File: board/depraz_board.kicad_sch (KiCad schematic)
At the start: 30 parts, among them J1 Switches, J2 Host, J3 SWD, U1 TLV75519PDRV, U2 TLV75533PDRV, U5 PMW3389DM, U6 STM32F103C8Tx, Y1 Crystal

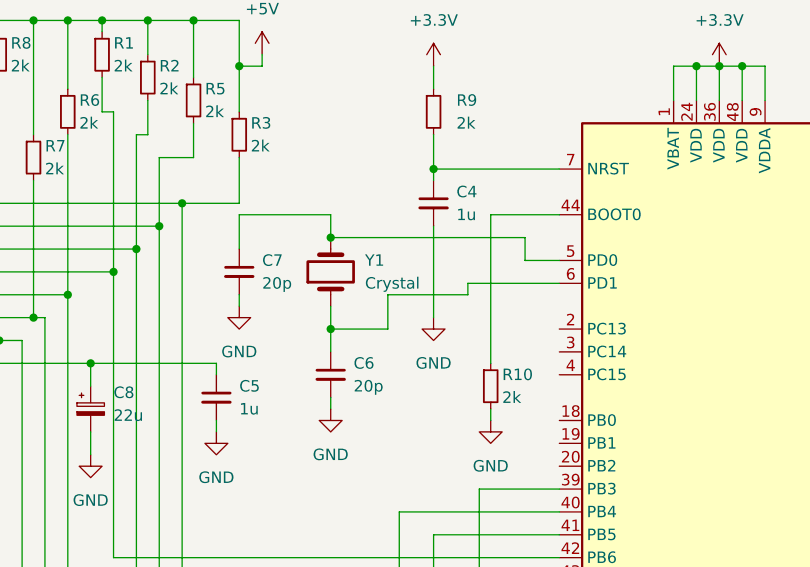
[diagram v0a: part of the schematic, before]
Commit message: Added LCSC part numbers for the SMD parts.
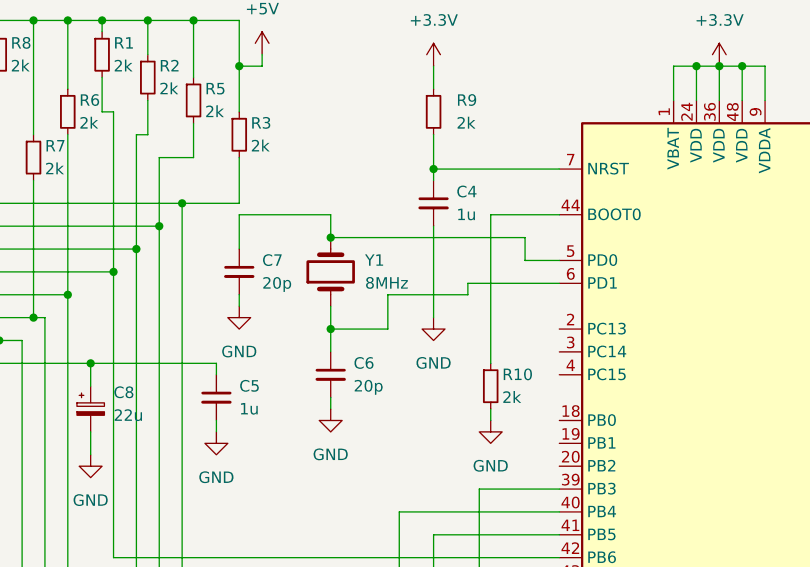
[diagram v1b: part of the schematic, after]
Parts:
- C1, C3, C4, C5: LCSC (none) -> C28323
- C2: LCSC (none) -> C1779
- C6, C7: LCSC (none) -> C1554
- C8: LCSC (none) -> C335975
- R1, R10, R2, R3, R5, R6, R7, R8, R9: LCSC (none) -> C4109
- R4: LCSC (none) -> C25282
- U1: LCSC (none) -> C2861631
- U2: LCSC (none) -> C2861750
- U6: LCSC (none) -> C8734
- Y1: value Crystal -> 8MHz; LCSC (none) -> C20617538
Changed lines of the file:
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@@
 			)
 		)
+		(property "LCSC" "C1779"
+			(at 266.7 102.87 0)
+			(effects
+				(font
+					(size 1.27 1.27)
+				)
+				(hide yes)
+			)
+		)
 		(pin "1"
 		)
@@
 			)
 		)
+		(property "LCSC" "C25282"
+			(at 214.63 107.95 90)
+			(effects
+				(font
+					(size 1.27 1.27)
+				)
+				(hide yes)
+			)
+		)
 		(pin "2"
 		)
@@
 			)
 		)
+		(property "LCSC" "C2861750"
+			(at 181.61 33.02 0)
+			(effects
+				(font
+					(size 1.27 1.27)
+				)
+				(hide yes)
+			)
+		)
 		(pin "6"
 		)
@@
 			)
 		)
+		(property "LCSC" "C1554"
+			(at 80.01 57.15 0)
+			(effects
+				(font
+					(size 1.27 1.27)
+				)
+				(hide yes)
+			)
+		)
 		(pin "1"
 		)
@@
 			)
 		)
+		(property "LCSC" "C4109"
+			(at 43.18 21.59 0)
+			(effects
+				(font
+					(size 1.27 1.27)
+				)
+				(hide yes)
+			)
+		)
 		(pin "1"
 		)
@@
 			)
 		)
+		(property "LCSC" "C8734"
+			(at 123.19 67.31 0)
+			(effects
+				(font
+					(size 1.27 1.27)
+				)
+				(hide yes)
+			)
+		)
 		(pin "47"
 		)
@@
 			)
 		)
+		(property "LCSC" "C4109"
+			(at 50.8 27.94 0)
+			(effects
+				(font
+					(size 1.27 1.27)
+				)
+				(hide yes)
+			)
+		)
 		(pin "1"
 		)
@@
 			)
 		)
+		(property "LCSC" "C4109"
+			(at 54.61 21.59 0)
+			(effects
+				(font
+					(size 1.27 1.27)
+				)
+				(hide yes)
+			)
+		)
 		(pin "1"
 		)
@@
 			)
 		)
+		(property "LCSC" "C28323"
+			(at 191.77 35.56 0)
+			(effects
+				(font
+					(size 1.27 1.27)
+				)
+				(hide yes)
+			)
+		)
 		(pin "1"
 		)
@@
 			)
 		)
+		(property "LCSC" "C4109"
+			(at 91.44 27.94 0)
+			(effects
+				(font
+					(size 1.27 1.27)
+				)
+				(hide yes)
+			)
+		)
 		(pin "2"
 		)
@@
 			)
 		)
+		(property "LCSC" "C4109"
+			(at 64.77 26.67 0)
+			(effects
+				(font
+					(size 1.27 1.27)
+				)
+				(hide yes)
+			)
+		)
 		(pin "1"
 		)
@@
 			)
 		)
+		(property "LCSC" "C4109"
+			(at 97.79 58.42 0)
+			(effects
+				(font
+					(size 1.27 1.27)
+				)
+				(hide yes)
+			)
+		)
 		(pin "1"
 		)
@@
 			)
 		)
+		(property "LCSC" "C28323"
+			(at 67.31 59.69 0)
+			(effects
+				(font
+					(size 1.27 1.27)
+				)
+				(hide yes)
+			)
+		)
 		(pin "1"
 		)
@@
 			)
 		)
+		(property "LCSC" "C28323"
+			(at 222.25 35.56 0)
+			(effects
+				(font
+					(size 1.27 1.27)
+				)
+				(hide yes)
+			)
+		)
 		(pin "2"
 		)
@@
 			)
 		)
+		(property "LCSC" "C1554"
+			(at 69.85 45.72 0)
+			(effects
+				(font
+					(size 1.27 1.27)
+				)
+				(hide yes)
+			)
+		)
 		(pin "1"
 		)
@@
 			)
 		)
+		(property "LCSC" "C28323"
+			(at 91.44 38.1 0)
+			(effects
+				(font
+					(size 1.27 1.27)
+				)
+				(hide yes)
+			)
+		)
 		(pin "1"
 		)
@@
 			)
 		)
+		(property "LCSC" "C4109"
+			(at 59.69 24.13 0)
+			(effects
+				(font
+					(size 1.27 1.27)
+				)
+				(hide yes)
+			)
+		)
 		(pin "1"
 		)
@@
 			)
 		)
+		(property "LCSC" "C335975"
+			(at 53.34 60.96 0)
+			(effects
+				(font
+					(size 1.27 1.27)
+				)
+				(hide yes)
+			)
+		)
 		(pin "1"
 		)
@@
 			)
 		)
+		(property "LCSC" "C4109"
+			(at 46.99 33.02 0)
+			(effects
+				(font
+					(size 1.27 1.27)
+				)
+				(hide yes)
+			)
+		)
 		(pin "1"
 		)
@@
 			)
 		)
-		(property "Value" "Crystal"
+		(property "Value" "8MHz"
 			(at 83.82 46.9899 90)
 			(effects
@@
 			)
 		)
+		(property "LCSC" "C20617538"
+			(at 80.01 45.72 90)
+			(effects
+				(font
+					(size 1.27 1.27)
+				)
+				(hide yes)
+			)
+		)
 		(pin "2"
 		)
@@
 			)
 		)
+		(property "LCSC" "C4109"
+			(at 69.85 30.48 0)
+			(effects
+				(font
+					(size 1.27 1.27)
+				)
+				(hide yes)
+			)
+		)
 		(pin "1"
 		)
@@
 			(at 210.82 33.02 0)
 			(effects
+				(font
+					(size 1.27 1.27)
+				)
+				(hide yes)
+			)
+		)
+		(property "LCSC" "C2861631"
+			(at 210.82 33.02 0)
+			(effects

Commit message: Fixes after review.
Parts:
- added C10, C11, C12, C9: 100n, Capacitor_SMD:C_0402_1005Metric, symbol Device:C_Small
- added C14: 1u, Capacitor_SMD:C_0805_2012Metric, symbol Device:C_Small
- added C15: 100n, Capacitor_SMD:C_0201_0603Metric, symbol Device:C_Small
- added D1: 1.9V PWR, LED_SMD:LED_0603_1608Metric, symbol Device:LED_Small_Filled
- added D2: 3.3V PWR, LED_SMD:LED_0805_2012Metric, symbol Device:LED_Small_Filled
- added D3: LED, LED_SMD:LED_0805_2012Metric, symbol Device:LED_Small_Filled
- added J4: SERIAL, Connector_PinHeader_2.54mm:PinHeader_1x04_P2.54mm_Vertical, symbol Connector_Generic:Conn_01x04
- added R11: 47, Resistor_SMD:R_0603_1608Metric, symbol Device:R_Small
- added R13, R14: 510, Resistor_SMD:R_0402_1005Metric, symbol Device:R_Small
- C1, C3: value 1u -> 4.7u; footprint Capacitor_SMD:C_0805_2012Metric -> Capacitor_SMD:C_1206_3216Metric; LCSC C28323 -> C29823
- C2: value 4.7uF -> 4.7u; footprint Capacitor_SMD:C_0805_2012Metric -> Capacitor_SMD:C_1206_3216Metric; LCSC C1779 -> C29823
- C4: value 1u -> 100n; footprint Capacitor_SMD:C_0805_2012Metric -> Capacitor_SMD:C_0402_1005Metric; LCSC C28323 -> C1525
- C8: LCSC C335975 -> C3356
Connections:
- net +3.3V: now also C4.1, U1.4 (EN), U1.6 (IN), C12.1, C14.1, C9.1, J4.1 (Pin_1), R14.1
- net +5V: no longer U1.4 (EN), U1.6 (IN)
- net GND: now also C10.2, C11.2, C12.2, C14.2, C15.2, C9.2, D1.1 (K), D2.1 (K), D3.1 (K), J4.4 (Pin_4)
- net at U5.13 (NCS): now also U6.38 (PA15); no longer U6.12 (PA2)
- net at U6.2 (PC13): now also R13.1
- net at U6.30 (PA9): now also J4.2 (Pin_2)
- net at U6.31 (PA10): now also J4.3 (Pin_3)
- net at R9.2, U6.7 (NRST): now also C10.1; no longer C4.1
- net 1.9V renamed +1.9V
- net +1.9V: now also C11.1, C15.1, R11.1
- new net: D3.2 (A), R13.2
- new net: D1.2 (A), R11.2
- new net: D2.2 (A), R14.2
- no-connect marks 5 -> 21
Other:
- moved on the sheet: C1, C5, R10, R9, U1

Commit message: Fixed layout after review.
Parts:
- C15: footprint Capacitor_SMD:C_0201_0603Metric -> Capacitor_SMD:C_0402_1005Metric
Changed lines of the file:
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@@
 			)
 		)
-		(property "Footprint" "Capacitor_SMD:C_0201_0603Metric"
+		(property "Footprint" "Capacitor_SMD:C_0402_1005Metric"
 			(at 262.89 114.3 0)
 			(effects
